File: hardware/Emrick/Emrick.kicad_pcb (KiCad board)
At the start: 4 copper layers, 44.4 x 59.2 mm, 86 parts, among them J1 LED_STRIP_CONNECTOR, J3 Conn_02x05_Odd_Even, J4 BATT_CONN, P1 USB_C_Plug_USB2.0, Q1 Q_NMOS_GSD, Q2 Q_NMOS_GSD, Q3 Q_NMOS_GSD, SW1 SW_SPST, U1 74HCT541, U2 CC1310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

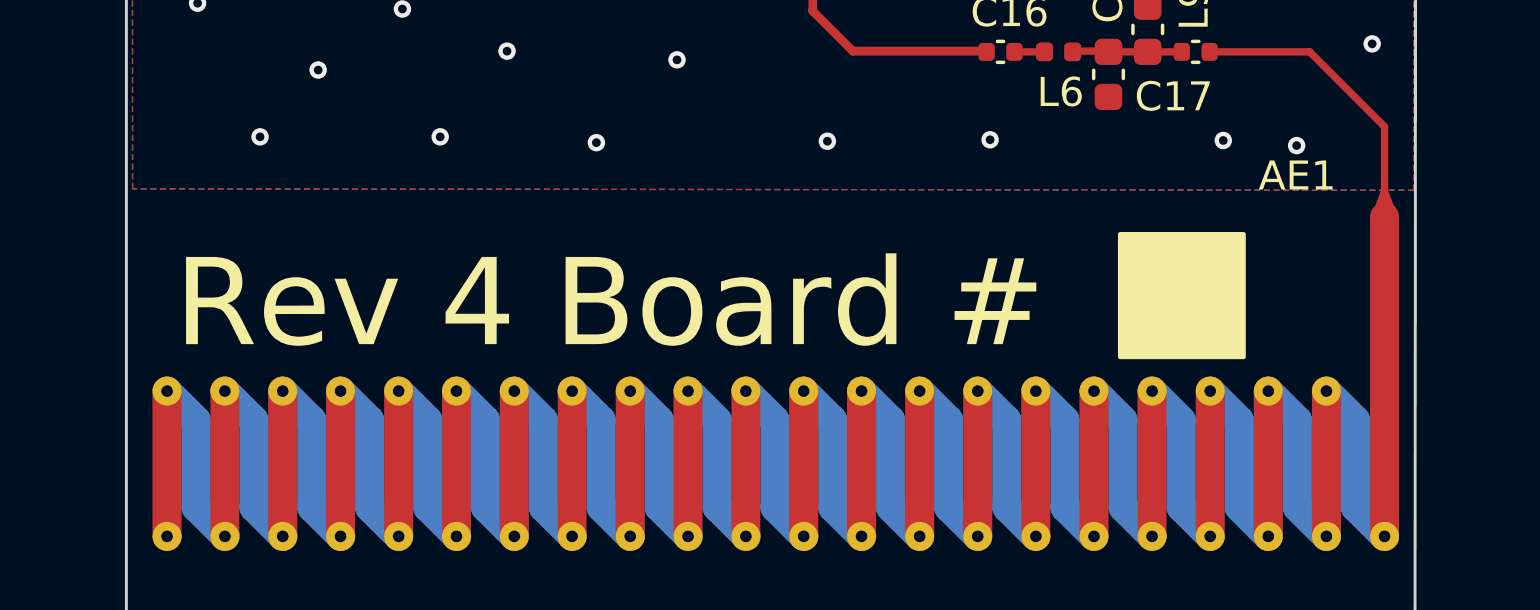
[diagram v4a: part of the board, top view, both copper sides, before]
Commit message: Update label and switch to an in-stock oscillator
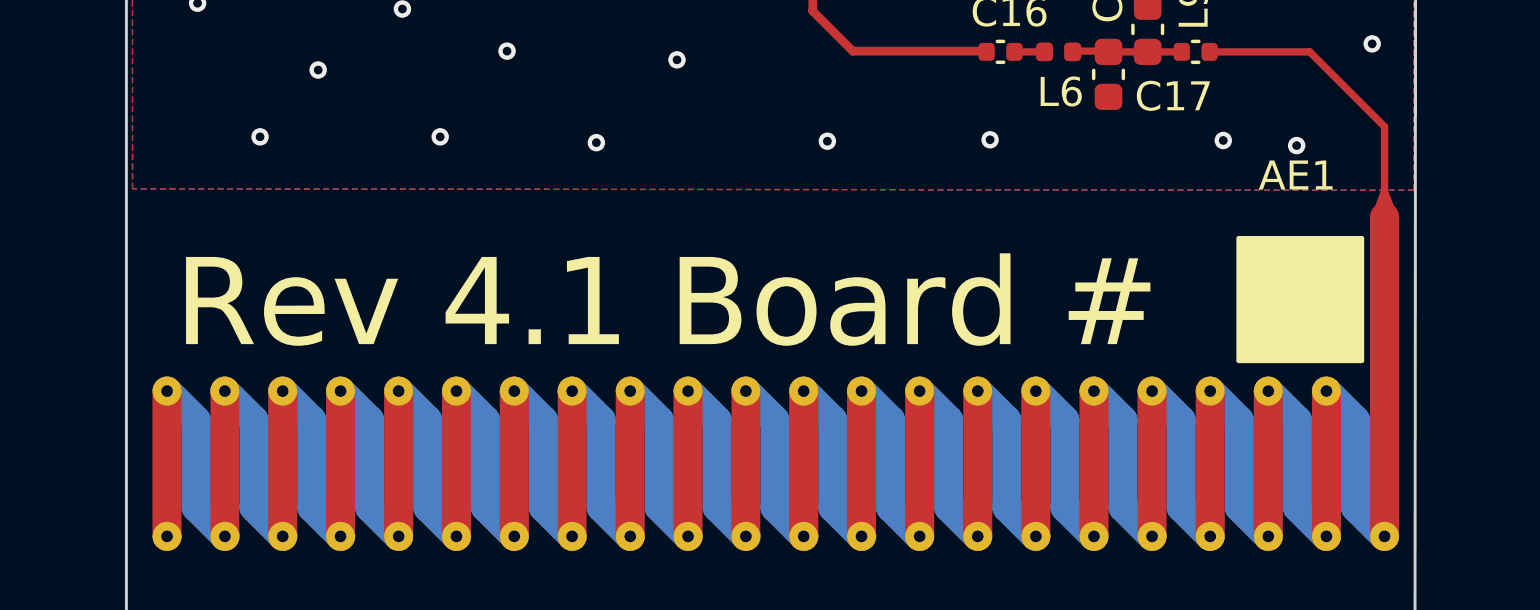
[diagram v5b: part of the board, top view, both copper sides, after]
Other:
- board text added: "Emrick Rev 4.1 8/20/2023"
- board text added: "Rev 4.1 Board #"
- board text removed: "Emrick Rev 4 7/29/2023"
- board text removed: "Rev 4 Board #"
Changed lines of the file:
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@@
   (gr_line (start 84.660056 60.515949) (end 84.677176 60.524391)
     (stroke (width 0.1) (type solid)) (layer "B.SilkS"))
-  (gr_rect (start 113 63.2) (end 117.25 67.425)
+  (gr_rect (start 117.075 63.3375) (end 121.325 67.5625)
     (stroke (width 0.15) (type solid)) (fill solid) (layer "F.SilkS"))
   (gr_rect (start 127.05 23.85) (end 168.55 75.85)
@@
   (gr_line (start 83.1 38.3) (end 122.4 38.4)
     (stroke (width 0.1) (type default)) (layer "B.Fab"))
-  (gr_text "Emrick Rev 4 7/29/2023\n" (at 100.9 44.575) (layer "B.SilkS")
+  (gr_text "Emrick Rev 4.1 8/20/2023\n" (at 100.9 44.575) (layer "B.SilkS")
     (effects (font (size 1.5 1.5) (thickness 0.3)) (justify mirror))
   )
@@
     (effects (font (size 1 1) (thickness 0.15)))
   )
-  (gr_text "Rev 4 Board #" (at 80.45 67.35) (layer "F.SilkS")
+  (gr_text "Rev 4.1 Board #" (at 80.45 67.35) (layer "F.SilkS")
     (effects (font (size 3 3) (thickness 0.3)) (justify left bottom))
   )

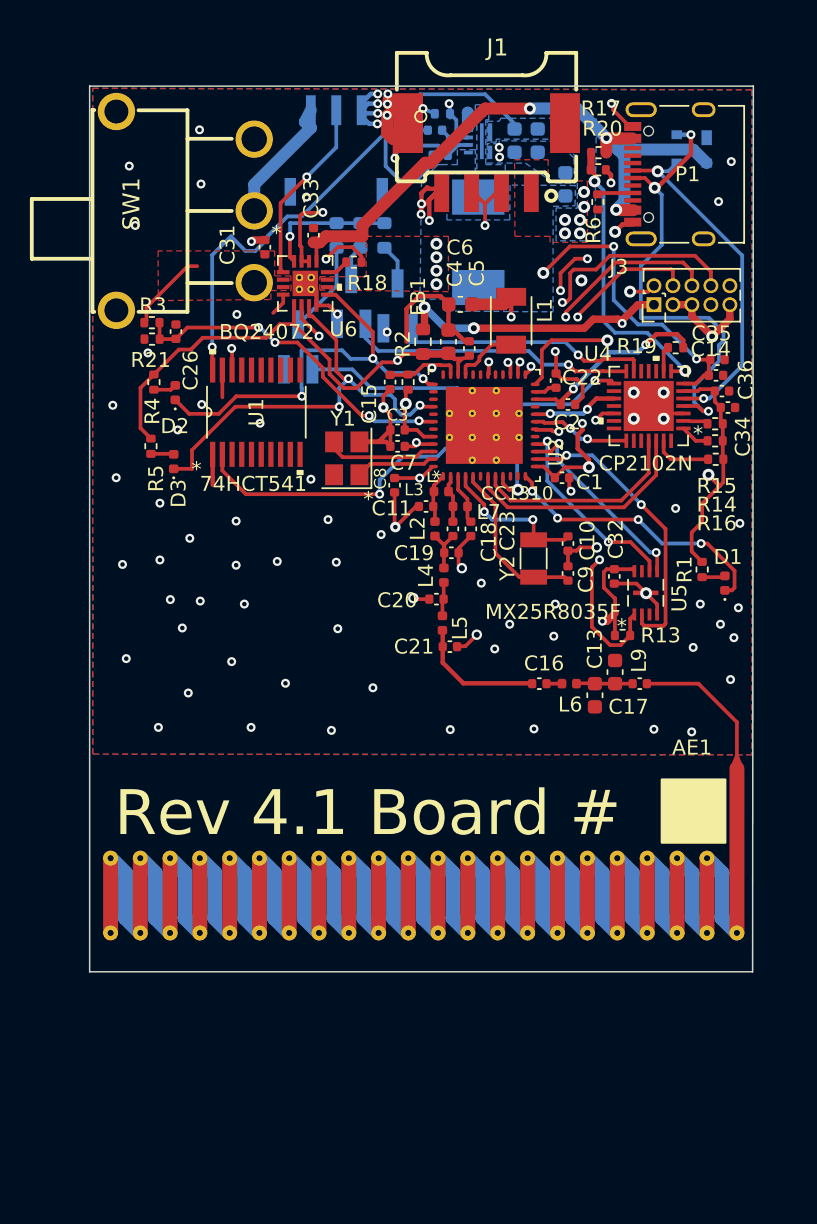
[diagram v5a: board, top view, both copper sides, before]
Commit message: Hardware modifications for rev 5
- Added control for battery charging to the microcontroller by connecting
CHARGE_ENABLE, BAT_EN1, and BAT_EN2 to pins on the micro.
- Modified the USB connector and schematic to support bidirectional USB insertion.
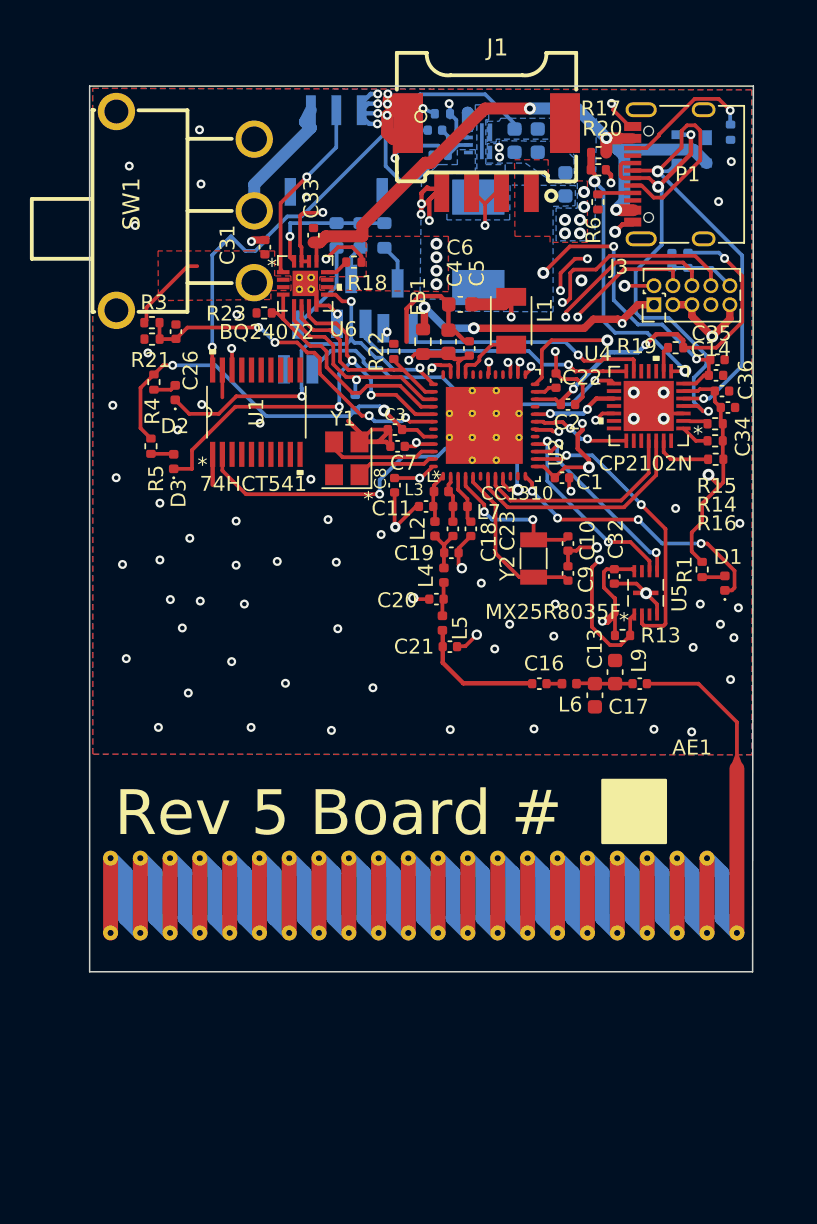
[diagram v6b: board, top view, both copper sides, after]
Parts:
- added R22: 10k, Resistor_SMD:R_0402_1005Metric, F.Cu at (99.2, 34.7)
- added R23: 10k, Resistor_SMD:R_0402_1005Metric, F.Cu at (90.5, 32.1)
- added R24: 10k, Resistor_SMD:R_0402_1005Metric, B.Cu at (96.6, 38.1)
- added R25: 5.1k, Resistor_SMD:R_0402_1005Metric, B.Cu at (121.7, 20.0)
- C15, R2: moved to B.Cu
- moved C15 20.5 mm to (117.8, 28.6), turned to 90 degrees
- moved R2 20.4 mm to (118.8, 28.6), turned to -90 degrees
- moved C3 0.18 mm to (99.2, 39.9)
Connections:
- P1 pad B5: unconnected-(P1-VCONN-PadB5) -> Net-(P1-VCONN)
- P1 pad B6: (no net) -> USB_DPLUS
- P1 pad B7: (no net) -> USB_DMINUS
- U2 pad 38: unconnected-(U2-DIO_25-Pad38) -> BAT_EN1
- U2 pad 39: unconnected-(U2-DIO_26-Pad39) -> BAT_EN2
- U2 pad 40: BAT_PGOOD -> CHARGE_EN
- U2 pad 41: unconnected-(U2-DIO_28-Pad41) -> BAT_PGOOD
- U6 pad 4: GND -> CHARGE_EN
- U6 pad 5: VDDS -> BAT_EN2
- U6 pad 6: GND -> BAT_EN1
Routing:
- net CHARGE_EN: track 0.00 -> 16.1 mm
- net BAT_EN2: track 0.00 -> 14.4 mm, vias 0 -> 1
- net BAT_EN1: track 0.00 -> 13.5 mm
- net USB_DMINUS: track 23.4 -> 36.2 mm
- net Net-(P1-VCONN): track 0.00 -> 8.91 mm, vias 0 -> 1
- net VDDS: track 118.0 -> 124.3 mm, vias 7 -> 9
- net GND: track 96.1 -> 92.9 mm, vias 93 -> 91
- net WMCU_RESET: track 42.5 -> 44.1 mm
- net CHR0: track 21.9 -> 23.1 mm
- net BAT_PGOOD: track 29.3 -> 30.2 mm
- net BAT_CHG: track 28.1 -> 27.4 mm
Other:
- board text added: "Emrick Rev 5 9/4/2023"
- board text added: "Rev 5 Board #"
- board text removed: "Emrick Rev 4.1 8/20/2023"
- board text removed: "Rev 4.1 Board #"

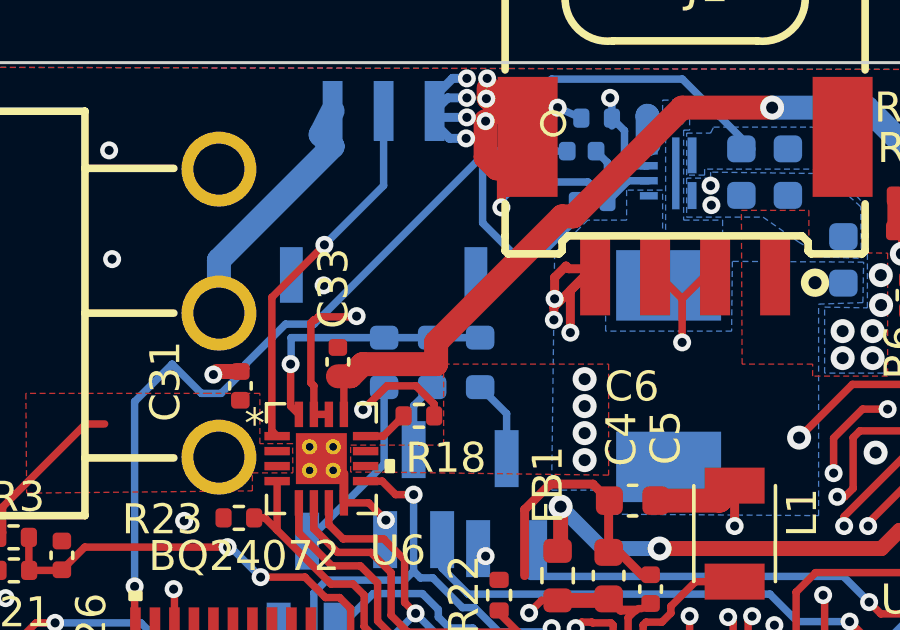
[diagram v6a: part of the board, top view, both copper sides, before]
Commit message: Add instructions for how to create the production files and how to verify the voltages on the PCB
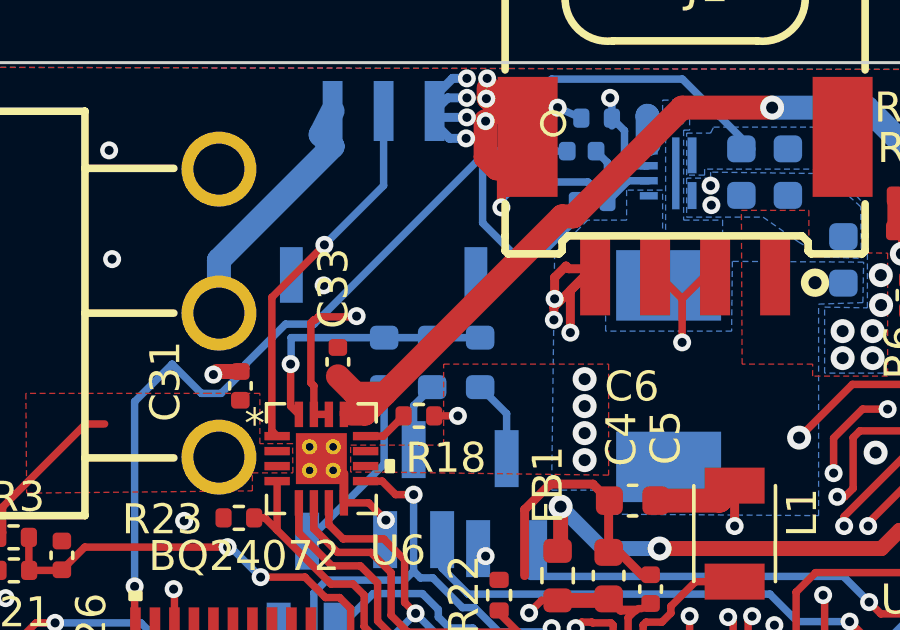
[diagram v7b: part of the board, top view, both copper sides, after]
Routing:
- net GND: track 92.9 -> 90.4 mm
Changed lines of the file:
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@@
   (segment (start 103.48 48.17) (end 103.48 47.87) (width 0.25) (layer "F.Cu") (net 2))
   (segment (start 117.82 31.575) (end 119.09 31.575) (width 0.5) (layer "F.Cu") (net 2))
-  (segment (start 96.985188 28.335) (end 96.375188 27.725) (width 0.25) (layer "F.Cu") (net 2))
   (segment (start 119.09 32.34) (end 120.45 33.7) (width 0.5) (layer "F.Cu") (net 2))
   (segment (start 116.762 52.2978) (end 116.762 51.612) (width 0.25) (layer "F.Cu") (net 2))
@@
   (segment (start 101 24.825) (end 101 24.11066) (width 0.3) (layer "F.Cu") (net 2))
   (segment (start 99.25 46.45) (end 100.63 45.07) (width 0.25) (layer "F.Cu") (net 2))
-  (segment (start 96.375188 27.725) (end 95.410612 27.725) (width 0.25) (layer "F.Cu") (net 2))
   (segment (start 98.8 18.125) (end 100.1 19.425) (width 0.8) (layer "F.Cu") (net 2))
   (segment (start 96.85 40.75) (end 98.62 40.75) (width 0.3) (layer "F.Cu") (net 2))
@@
   (segment (start 110.88 43.15) (end 110.88 43.93) (width 0.25) (layer "F.Cu") (net 2))
   (segment (start 99.225 20.3) (end 100.1 19.425) (width 0.3) (layer "F.Cu") (net 2))
-  (segment (start 96.985188 28.725) (end 96.985188 28.335) (width 0.25) (layer "F.Cu") (net 2))
   (segment (start 103.155 33.275) (end 103.95 34.07) (width 0.3) (layer "F.Cu") (net 2))
   (segment (start 93.025 25.525) (end 93.125 25.425) (width 0.25) (layer "F.Cu") (net 2))
   (segment (start 93.974999 30.646167) (end 93.974999 31.583831) (width 0.3) (layer "F.Cu") (net 2))
-  (segment (start 95.410612 27.725) (end 94.614688 28.520924) (width 0.25) (layer "F.Cu") (net 2))
+  (segment (start 96.985188 28.725) (end 97.775 28.725) (width 0.25) (layer "F.Cu") (net 2))
   (segment (start 93.975188 31.625) (end 94.8 31.625) (width 0.25) (layer "F.Cu") (net 2))
   (segment (start 113.9 50.23) (end 115.38 50.23) (width 0.25) (layer "F.Cu") (net 2))
@@
   (via (at 91.9 56.9) (size 0.6) (drill 0.3) (layers "F.Cu" "B.Cu") (free) (net 2))
   (via (at 108.525 59.95) (size 0.6) (drill 0.3) (layers "F.Cu" "B.Cu") (free) (net 2))
-  (via (at 94.614688 28.520924) (size 0.6) (drill 0.3) (layers "F.Cu" "B.Cu") (net 2))
   (via (at 97.75 57.2) (size 0.6) (drill 0.3) (layers "F.Cu" "B.Cu") (free) (net 2))
   (via (at 88.3 55.45) (size 0.6) (drill 0.3) (layers "F.Cu" "B.Cu") (free) (net 2))
@@
   (via (at 80.575 43.15) (size 0.6) (drill 0.3) (layers "F.Cu" "B.Cu") (free) (net 2))
   (via (at 105 50.2) (size 0.6) (drill 0.3) (layers "F.Cu" "B.Cu") (free) (net 2))
+  (via (at 97.775 28.725) (size 0.6) (drill 0.3) (layers "F.Cu" "B.Cu") (net 2))
   (via (at 101 24.825) (size 0.6) (drill 0.3) (layers "F.Cu" "B.Cu") (free) (net 2))
   (via (at 81.45 22.3) (size 0.6) (drill 0.3) (layers "F.Cu" "B.Cu") (free) (net 2))
@@
   (segment (start 122.1 59.5) (end 122.1 61.775) (width 0.25) (layer "F.Cu") (net 8))
   (segment (start 119.525 56.925) (end 122.1 59.5) (width 0.25) (layer "F.Cu") (net 8))
-  (segment (start 93.775188 27.405) (end 94.195 27.405) (width 0.8) (layer "F.Cu") (net 9))
   (segment (start 113.36 21.4) (end 113.36 20.44) (width 0.8) (layer "F.Cu") (net 9))
   (segment (start 113.4 20.45) (end 113.375 20.425) (width 0.8) (layer "F.Cu") (net 9))
   (segment (start 115.13 25.1) (end 115.13 25.4) (width 0.25) (layer "F.Cu") (net 9))
-  (segment (start 101.25 22.075) (end 101.625 22.075) (width 0.8) (layer "F.Cu") (net 9))
-  (segment (start 97.05 26.275) (end 101.25 22.075) (width 0.8) (layer "F.Cu") (net 9))
-  (segment (start 93.975188 28.674998) (end 93.975188 27.605) (width 0.25) (layer "F.Cu") (net 9))
+  (segment (start 101.625 22.075) (end 105.25 18.45) (width 0.8) (layer "F.Cu") (net 9))
+  (segment (start 94.357688 27.9875) (end 93.775188 27.405) (width 0.8) (layer "F.Cu") (net 9))
+  (segment (start 105.25 18.45) (end 108.25 18.45) (width 0.8) (layer "F.Cu") (net 9))
   (segment (start 113.36 20.44) (end 113.375 20.425) (width 0.8) (layer "F.Cu") (net 9))
   (segment (start 114.2625 20.45) (end 115.1375 20.45) (width 0.7) (layer "F.Cu") (net 9))
-  (segment (start 97.05 27) (end 97.05 26.275) (width 0.8) (layer "F.Cu") (net 9))
+  (segment (start 95.3375 27.9875) (end 94.357688 27.9875) (width 0.8) (layer "F.Cu") (net 9))
   (segment (start 113.4875 20.45) (end 113.4 20.45) (width 0.8) (layer "F.Cu") (net 9))
-  (segment (start 105.25 18.45) (end 108.25 18.45) (width 0.8) (layer "F.Cu") (net 9))
+  (segment (start 95.3375 27.9875) (end 101.25 22.075) (width 0.8) (layer "F.Cu") (net 9))
+  (segment (start 94.975188 28.349812) (end 95.3375 27.9875) (width 0.8) (layer "F.Cu") (net 9))
   (segment (start 113.4875 20.45) (end 114.2625 20.45) (width 0.8) (layer "F.Cu") (net 9))
+  (segment (start 101.25 22.075) (end 101.625 22.075) (width 0.8) (layer "F.Cu") (net 9))
+  (segment (start 94.675 28.65) (end 94.225 28.65) (width 0.8) (layer "F.Cu") (net 9))
   (segment (start 114.3125 25.25) (end 115.1875 25.25) (width 0.8) (layer "F.Cu") (net 9))
   (segment (start 93.975188 27.605) (end 93.775188 27.405) (width 0.25) (layer "F.Cu") (net 9))
-  (segment (start 94.6 27) (end 97.05 27) (width 0.8) (layer "F.Cu") (net 9))
-  (segment (start 101.625 22.075) (end 105.25 18.45) (width 0.8) (layer "F.Cu") (net 9))
-  (segment (start 94.195 27.405) (end 94.6 27) (width 0.8) (layer "F.Cu") (net 9))
+  (segment (start 94.975188 28.349812) (end 94.675 28.65) (width 0.8) (layer "F.Cu") (net 9))
   (via (at 114.025 25.225) (size 0.8) (drill 0.4) (layers "F.Cu" "B.Cu") (net 9))
   (via (at 113.375 20.425) (size 0.8) (drill 0.4) (layers "F.Cu" "B.Cu") (net 9))
@@
   (via (at 105.25 26.275) (size 0.6) (drill 0.3) (layers "F.Cu" "B.Cu") (net 25))
   (via (at 88.3 34.5) (size 0.6) (drill 0.3) (layers "F.Cu" "B.Cu") (net 25))
-  (segment (start 100.25 26.775) (end 104.75 26.775) (width 0.25) (layer "In1.Cu") (net 25))
-  (segment (start 99.4 26.825) (end 100.2 26.825) (width 0.25) (layer "In1.Cu") (net 25))
+  (segment (start 90.941116 33.475) (end 91.5 33.475) (width 0.25) (layer "In1.Cu") (net 25))
+  (segment (start 91.5 33.475) (end 98.2 26.775) (width 0.25) (layer "In1.Cu") (net 25))
+  (segment (start 90.25 34.166116) (end 90.941116 33.475) (width 0.25) (layer "In1.Cu") (net 25))
+  (segment (start 90.25 34.725) (end 90.25 34.166116) (width 0.25) (layer "In1.Cu") (net 25))
   (segment (start 104.75 26.775) (end 105.25 26.275) (width 0.25) (layer "In1.Cu") (net 25))
-  (segment (start 100.2 26.825) (end 100.25 26.775) (width 0.25) (layer "In1.Cu") (net 25))
-  (segment (start 88.525 34.725) (end 91.5 34.725) (width 0.25) (layer "In1.Cu") (net 25))
+  (segment (start 98.2 26.775) (end 104.75 26.775) (width 0.25) (layer "In1.Cu") (net 25))
   (segment (start 88.3 34.5) (end 88.525 34.725) (width 0.25) (layer "In1.Cu") (net 25))
-  (segment (start 91.5 34.725) (end 99.4 26.825) (width 0.25) (layer "In1.Cu") (net 25))
+  (segment (start 88.525 34.725) (end 90.25 34.725) (width 0.25) (layer "In1.Cu") (net 25))
   (segment (start 108.600001 36.9) (end 109.050001 36.45) (width 0.25) (layer "F.Cu") (net 26))
   (segment (start 109.7 33.95) (end 113.425402 33.95) (width 0.25) (layer "F.Cu") (net 26))
